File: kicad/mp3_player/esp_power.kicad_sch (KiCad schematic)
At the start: 12 parts, among them J1 Conn_USB_C_Socket, U5 AMS1117-3.3

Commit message: [ADD] an initial set of libraries to depressed to do their own job
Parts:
- renumbered C3 to C4, C4 to C5, C5 to C6, C6 to C7, C7 to C8, J1 to J2, R6 to R11, R7 to R12, R8 to R13, R9 to R14, R10 to R15
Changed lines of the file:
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@@
 		(dnp no)
 		(fields_autoplaced yes)
-		(property "Reference" "#PWR016"
+		(property "Reference" "#PWR019"
 			(at 43.18 78.74 0)
 			(hide yes)
@@
 			(project "mp3_player"
 				(path "/0f0043d3-9467-400d-886a-57a73f910f34/68afa0b0-fbce-4e06-b0d1-6752d3bde468"
-					(reference "#PWR016")
+					(reference "#PWR019")
 					(unit 1)
 				)
@@
 		(in_pos_files yes)
 		(dnp no)
-		(property "Reference" "R8"
+		(property "Reference" "R13"
 			(at 61.976 48.514 0)
 			(show_name no)
@@
 			(project "mp3_player"
 				(path "/0f0043d3-9467-400d-886a-57a73f910f34/68afa0b0-fbce-4e06-b0d1-6752d3bde468"
-					(reference "R8")
+					(reference "R13")
 					(unit 1)
 				)
@@
 		(dnp no)
 		(fields_autoplaced yes)
-		(property "Reference" "#PWR017"
+		(property "Reference" "#PWR020"
 			(at 73.66 40.64 0)
 			(hide yes)
@@
 			(project "mp3_player"
 				(path "/0f0043d3-9467-400d-886a-57a73f910f34/68afa0b0-fbce-4e06-b0d1-6752d3bde468"
-					(reference "#PWR017")
+					(reference "#PWR020")
 					(unit 1)
 				)
@@
 		(dnp no)
 		(fields_autoplaced yes)
-		(property "Reference" "R6"
+		(property "Reference" "R11"
 			(at 54.61 63.5 0)
 			(show_name no)
@@
 			(project "mp3_player"
 				(path "/0f0043d3-9467-400d-886a-57a73f910f34/68afa0b0-fbce-4e06-b0d1-6752d3bde468"
-					(reference "R6")
+					(reference "R11")
 					(unit 1)
 				)
@@
 		(dnp no)
 		(fields_autoplaced yes)
-		(property "Reference" "#PWR019"
+		(property "Reference" "#PWR022"
 			(at 74.93 31.75 0)
 			(hide yes)
@@
 			(project "mp3_player"
 				(path "/0f0043d3-9467-400d-886a-57a73f910f34/68afa0b0-fbce-4e06-b0d1-6752d3bde468"
-					(reference "#PWR019")
+					(reference "#PWR022")
 					(unit 1)
 				)
@@
 		(in_pos_files yes)
 		(dnp no)
-		(property "Reference" "C3"
+		(property "Reference" "C4"
 			(at 54.61 77.47 0)
 			(show_name no)
@@
 			(project "mp3_player"
 				(path "/0f0043d3-9467-400d-886a-57a73f910f34/68afa0b0-fbce-4e06-b0d1-6752d3bde468"
-					(reference "C3")
+					(reference "C4")
 					(unit 1)
 				)
@@
 		(dnp no)
 		(fields_autoplaced yes)
-		(property "Reference" "J1"
+		(property "Reference" "J2"
 			(at 25.4 49.5299 0)
 			(show_name no)
@@
 			(project "mp3_player"
 				(path "/0f0043d3-9467-400d-886a-57a73f910f34/68afa0b0-fbce-4e06-b0d1-6752d3bde468"
-					(reference "J1")
+					(reference "J2")
 					(unit 1)
 				)
@@
 		(dnp no)
 		(fields_autoplaced yes)
-		(property "Reference" "#PWR020"
+		(property "Reference" "#PWR023"
 			(at 74.93 59.69 0)
 			(hide yes)
@@
 			(project "mp3_player"
 				(path "/0f0043d3-9467-400d-886a-57a73f910f34/68afa0b0-fbce-4e06-b0d1-6752d3bde468"
-					(reference "#PWR020")
+					(reference "#PWR023")
 					(unit 1)
 				)
@@
 		(dnp no)
 		(fields_autoplaced yes)
-		(property "Reference" "#PWR021"
+		(property "Reference" "#PWR024"
 			(at 85.09 76.2 0)
 			(hide yes)
@@
 			(project "mp3_player"
 				(path "/0f0043d3-9467-400d-886a-57a73f910f34/68afa0b0-fbce-4e06-b0d1-6752d3bde468"
-					(reference "#PWR021")
+					(reference "#PWR024")
 					(unit 1)
 				)
@@
 		(dnp no)
 		(fields_autoplaced yes)
-		(property "Reference" "#PWR022"
+		(property "Reference" "#PWR025"
 			(at 105.41 48.26 0)
 			(hide yes)
@@
 			(project "mp3_player"
 				(path "/0f0043d3-9467-400d-886a-57a73f910f34/68afa0b0-fbce-4e06-b0d1-6752d3bde468"
-					(reference "#PWR022")
+					(reference "#PWR025")
 					(unit 1)
 				)
@@
 		(in_pos_files yes)
 		(dnp no)
-		(property "Reference" "C4"
+		(property "Reference" "C5"
 			(at 77.47 40.64 0)
 			(show_name no)
@@
 			(project "mp3_player"
 				(path "/0f0043d3-9467-400d-886a-57a73f910f34/68afa0b0-fbce-4e06-b0d1-6752d3bde468"
-					(reference "C4")
+					(reference "C5")
 					(unit 1)
 				)
@@
 		(in_pos_files yes)
 		(dnp no)
-		(property "Reference" "C7"
+		(property "Reference" "C8"
 			(at 101.6 54.61 0)
 			(show_name no)
@@
 			(project "mp3_player"
 				(path "/0f0043d3-9467-400d-886a-57a73f910f34/68afa0b0-fbce-4e06-b0d1-6752d3bde468"
-					(reference "C7")
+					(reference "C8")
 					(unit 1)
 				)
@@
 		(in_pos_files yes)
 		(dnp no)
-		(property "Reference" "C6"
+		(property "Reference" "C7"
 			(at 97.79 67.31 0)
 			(show_name no)
@@
 			(project "mp3_player"
 				(path "/0f0043d3-9467-400d-886a-57a73f910f34/68afa0b0-fbce-4e06-b0d1-6752d3bde468"
-					(reference "C6")
+					(reference "C7")
 					(unit 1)
 				)
@@
 		(in_pos_files yes)
 		(dnp no)
-		(property "Reference" "C5"
+		(property "Reference" "C6"
 			(at 88.9 67.31 0)
 			(show_name no)
@@
 			(project "mp3_player"
 				(path "/0f0043d3-9467-400d-886a-57a73f910f34/68afa0b0-fbce-4e06-b0d1-6752d3bde468"
-					(reference "C5")
+					(reference "C6")
 					(unit 1)
 				)
@@
 		(in_pos_files yes)
 		(dnp no)
-		(property "Reference" "R10"
+		(property "Reference" "R15"
 			(at 111.78 52.07 0)
 			(show_name no)
@@
 			(project "mp3_player"
 				(path "/0f0043d3-9467-400d-886a-57a73f910f34/68afa0b0-fbce-4e06-b0d1-6752d3bde468"
-					(reference "R10")
+					(reference "R15")
 					(unit 1)
 				)
@@
 		(in_pos_files yes)
 		(dnp no)
-		(property "Reference" "R9"
+		(property "Reference" "R14"
 			(at 111.76 46.99 0)
 			(show_name no)
@@
 			(project "mp3_player"
 				(path "/0f0043d3-9467-400d-886a-57a73f910f34/68afa0b0-fbce-4e06-b0d1-6752d3bde468"
-					(reference "R9")
+					(reference "R14")
 					(unit 1)
 				)
@@
 		(in_pos_files yes)
 		(dnp no)
-		(property "Reference" "R7"
+		(property "Reference" "R12"
 			(at 62.23 39.116 0)
 			(show_name no)
@@
 			(project "mp3_player"
 				(path "/0f0043d3-9467-400d-886a-57a73f910f34/68afa0b0-fbce-4e06-b0d1-6752d3bde468"
-					(reference "R7")
+					(reference "R12")
 					(unit 1)
 				)
@@
 		(dnp no)
 		(fields_autoplaced yes)
-		(property "Reference" "#PWR018"
+		(property "Reference" "#PWR021"
 			(at 73.66 43.18 0)
 			(hide yes)
@@
 			(project "mp3_player"
 				(path "/0f0043d3-9467-400d-886a-57a73f910f34/68afa0b0-fbce-4e06-b0d1-6752d3bde468"
-					(reference "#PWR018")
-					(unit 1)
-				)
+					(reference "#PWR021")
+					(unit 1)
+				)

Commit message: [UPDATE] the desing of the schematic to use the current audio module
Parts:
- renumbered C4 to C2, C5 to C3, C6 to C4, C7 to C5, C8 to C6
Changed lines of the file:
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@@
 		(dnp no)
 		(fields_autoplaced yes)
-		(property "Reference" "#PWR019"
+		(property "Reference" "#PWR017"
 			(at 43.18 78.74 0)
 			(hide yes)
@@
 			(project "mp3_player"
 				(path "/0f0043d3-9467-400d-886a-57a73f910f34/68afa0b0-fbce-4e06-b0d1-6752d3bde468"
-					(reference "#PWR019")
+					(reference "#PWR017")
 					(unit 1)
 				)
@@
 		(dnp no)
 		(fields_autoplaced yes)
-		(property "Reference" "#PWR020"
+		(property "Reference" "#PWR018"
 			(at 73.66 40.64 0)
 			(hide yes)
@@
 			(project "mp3_player"
 				(path "/0f0043d3-9467-400d-886a-57a73f910f34/68afa0b0-fbce-4e06-b0d1-6752d3bde468"
-					(reference "#PWR020")
+					(reference "#PWR018")
 					(unit 1)
 				)
@@
 		(dnp no)
 		(fields_autoplaced yes)
-		(property "Reference" "#PWR022"
+		(property "Reference" "#PWR020"
 			(at 74.93 31.75 0)
 			(hide yes)
@@
 			(project "mp3_player"
 				(path "/0f0043d3-9467-400d-886a-57a73f910f34/68afa0b0-fbce-4e06-b0d1-6752d3bde468"
-					(reference "#PWR022")
+					(reference "#PWR020")
 					(unit 1)
 				)
@@
 		(in_pos_files yes)
 		(dnp no)
-		(property "Reference" "C4"
+		(property "Reference" "C2"
 			(at 54.61 77.47 0)
 			(show_name no)
@@
 			(project "mp3_player"
 				(path "/0f0043d3-9467-400d-886a-57a73f910f34/68afa0b0-fbce-4e06-b0d1-6752d3bde468"
-					(reference "C4")
+					(reference "C2")
 					(unit 1)
 				)
@@
 		(dnp no)
 		(fields_autoplaced yes)
-		(property "Reference" "#PWR023"
+		(property "Reference" "#PWR021"
 			(at 74.93 59.69 0)
 			(hide yes)
@@
 			(project "mp3_player"
 				(path "/0f0043d3-9467-400d-886a-57a73f910f34/68afa0b0-fbce-4e06-b0d1-6752d3bde468"
-					(reference "#PWR023")
+					(reference "#PWR021")
 					(unit 1)
 				)
@@
 		(dnp no)
 		(fields_autoplaced yes)
-		(property "Reference" "#PWR024"
+		(property "Reference" "#PWR022"
 			(at 85.09 76.2 0)
 			(hide yes)
@@
 			(project "mp3_player"
 				(path "/0f0043d3-9467-400d-886a-57a73f910f34/68afa0b0-fbce-4e06-b0d1-6752d3bde468"
-					(reference "#PWR024")
+					(reference "#PWR022")
 					(unit 1)
 				)
@@
 		(dnp no)
 		(fields_autoplaced yes)
-		(property "Reference" "#PWR025"
+		(property "Reference" "#PWR023"
 			(at 105.41 48.26 0)
 			(hide yes)
@@
 			(project "mp3_player"
 				(path "/0f0043d3-9467-400d-886a-57a73f910f34/68afa0b0-fbce-4e06-b0d1-6752d3bde468"
-					(reference "#PWR025")
+					(reference "#PWR023")
 					(unit 1)
 				)
@@
 		(in_pos_files yes)
 		(dnp no)
-		(property "Reference" "C5"
+		(property "Reference" "C3"
 			(at 77.47 40.64 0)
 			(show_name no)
@@
 			(project "mp3_player"
 				(path "/0f0043d3-9467-400d-886a-57a73f910f34/68afa0b0-fbce-4e06-b0d1-6752d3bde468"
-					(reference "C5")
+					(reference "C3")
 					(unit 1)
 				)
@@
 		(in_pos_files yes)
 		(dnp no)
-		(property "Reference" "C8"
+		(property "Reference" "C6"
 			(at 101.6 54.61 0)
 			(show_name no)
@@
 			(project "mp3_player"
 				(path "/0f0043d3-9467-400d-886a-57a73f910f34/68afa0b0-fbce-4e06-b0d1-6752d3bde468"
-					(reference "C8")
+					(reference "C6")
 					(unit 1)
 				)
@@
 		(in_pos_files yes)
 		(dnp no)
-		(property "Reference" "C7"
+		(property "Reference" "C5"
 			(at 97.79 67.31 0)
 			(show_name no)
@@
 			(project "mp3_player"
 				(path "/0f0043d3-9467-400d-886a-57a73f910f34/68afa0b0-fbce-4e06-b0d1-6752d3bde468"
-					(reference "C7")
+					(reference "C5")
 					(unit 1)
 				)
@@
 		(in_pos_files yes)
 		(dnp no)
-		(property "Reference" "C6"
+		(property "Reference" "C4"
 			(at 88.9 67.31 0)
 			(show_name no)
@@
 			(project "mp3_player"
 				(path "/0f0043d3-9467-400d-886a-57a73f910f34/68afa0b0-fbce-4e06-b0d1-6752d3bde468"
-					(reference "C6")
+					(reference "C4")
 					(unit 1)
 				)
@@
 		(dnp no)
 		(fields_autoplaced yes)
-		(property "Reference" "#PWR021"
+		(property "Reference" "#PWR019"
 			(at 73.66 43.18 0)
 			(hide yes)
@@
 			(project "mp3_player"
 				(path "/0f0043d3-9467-400d-886a-57a73f910f34/68afa0b0-fbce-4e06-b0d1-6752d3bde468"
-					(reference "#PWR021")
-					(unit 1)
-				)
+					(reference "#PWR019")
+					(unit 1)
+				)

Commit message: [ADD] lcd segment displays to the project
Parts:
- renumbered J2 to J4
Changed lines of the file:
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@@
 		(dnp no)
 		(fields_autoplaced yes)
-		(property "Reference" "#PWR017"
+		(property "Reference" "#PWR020"
 			(at 43.18 78.74 0)
 			(hide yes)
@@
 			(project "mp3_player"
 				(path "/0f0043d3-9467-400d-886a-57a73f910f34/68afa0b0-fbce-4e06-b0d1-6752d3bde468"
-					(reference "#PWR017")
+					(reference "#PWR020")
 					(unit 1)
 				)
@@
 		(dnp no)
 		(fields_autoplaced yes)
-		(property "Reference" "#PWR018"
+		(property "Reference" "#PWR021"
 			(at 73.66 40.64 0)
 			(hide yes)
@@
 			(project "mp3_player"
 				(path "/0f0043d3-9467-400d-886a-57a73f910f34/68afa0b0-fbce-4e06-b0d1-6752d3bde468"
-					(reference "#PWR018")
+					(reference "#PWR021")
 					(unit 1)
 				)
@@
 		(dnp no)
 		(fields_autoplaced yes)
-		(property "Reference" "#PWR020"
+		(property "Reference" "#PWR023"
 			(at 74.93 31.75 0)
 			(hide yes)
@@
 			(project "mp3_player"
 				(path "/0f0043d3-9467-400d-886a-57a73f910f34/68afa0b0-fbce-4e06-b0d1-6752d3bde468"
-					(reference "#PWR020")
+					(reference "#PWR023")
 					(unit 1)
 				)
@@
 		(dnp no)
 		(fields_autoplaced yes)
-		(property "Reference" "J2"
+		(property "Reference" "J4"
 			(at 25.4 49.5299 0)
 			(show_name no)
@@
 			(project "mp3_player"
 				(path "/0f0043d3-9467-400d-886a-57a73f910f34/68afa0b0-fbce-4e06-b0d1-6752d3bde468"
-					(reference "J2")
+					(reference "J4")
 					(unit 1)
 				)
@@
 		(dnp no)
 		(fields_autoplaced yes)
-		(property "Reference" "#PWR021"
+		(property "Reference" "#PWR024"
 			(at 74.93 59.69 0)
 			(hide yes)
@@
 			(project "mp3_player"
 				(path "/0f0043d3-9467-400d-886a-57a73f910f34/68afa0b0-fbce-4e06-b0d1-6752d3bde468"
-					(reference "#PWR021")
+					(reference "#PWR024")
 					(unit 1)
 				)
@@
 		(dnp no)
 		(fields_autoplaced yes)
-		(property "Reference" "#PWR022"
+		(property "Reference" "#PWR025"
 			(at 85.09 76.2 0)
 			(hide yes)
@@
 			(project "mp3_player"
 				(path "/0f0043d3-9467-400d-886a-57a73f910f34/68afa0b0-fbce-4e06-b0d1-6752d3bde468"
-					(reference "#PWR022")
+					(reference "#PWR025")
 					(unit 1)
 				)
@@
 		(dnp no)
 		(fields_autoplaced yes)
-		(property "Reference" "#PWR023"
+		(property "Reference" "#PWR026"
 			(at 105.41 48.26 0)
 			(hide yes)
@@
 			(project "mp3_player"
 				(path "/0f0043d3-9467-400d-886a-57a73f910f34/68afa0b0-fbce-4e06-b0d1-6752d3bde468"
-					(reference "#PWR023")
+					(reference "#PWR026")
 					(unit 1)
 				)
@@
 		(dnp no)
 		(fields_autoplaced yes)
-		(property "Reference" "#PWR019"
+		(property "Reference" "#PWR022"
 			(at 73.66 43.18 0)
 			(hide yes)
@@
 			(project "mp3_player"
 				(path "/0f0043d3-9467-400d-886a-57a73f910f34/68afa0b0-fbce-4e06-b0d1-6752d3bde468"
-					(reference "#PWR019")
-					(unit 1)
-				)
+					(reference "#PWR022")
+					(unit 1)
+				)

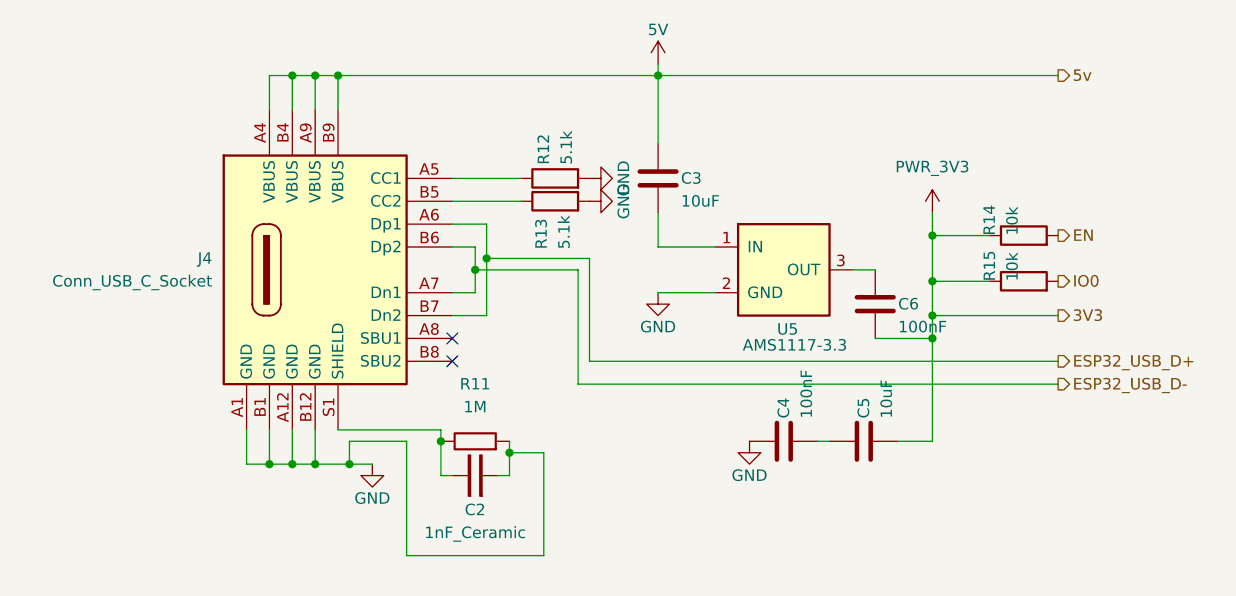
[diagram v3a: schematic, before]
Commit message: [UPDATE] the schematic to include the power help to avoid a crash or lcd corruption due to brown outs
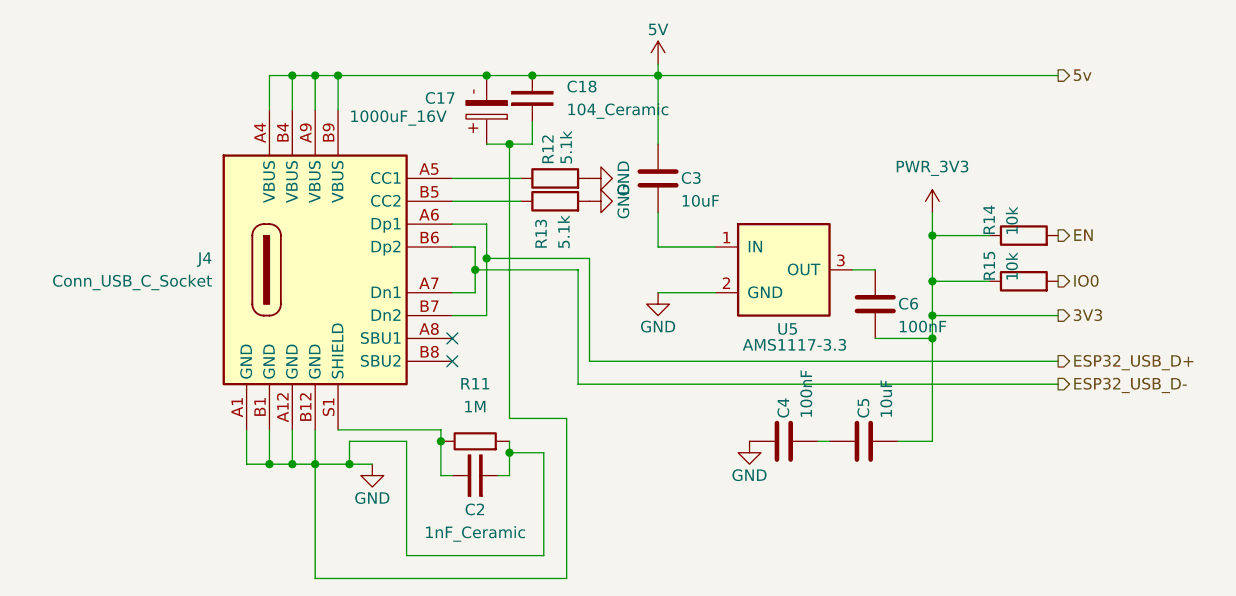
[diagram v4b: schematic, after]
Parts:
- added C17: 1000uF_16V, Capacitor_THT:CP_Radial_D10.0mm_P5.00mm, symbol PCM_SL_Capacitors:1000uF_16V
- added C18: 104_Ceramic, Capacitor_THT:C_Disc_D5.0mm_W2.5mm_P2.50mm, symbol PCM_SL_Capacitors:104_Ceramic
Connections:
- net 5V: now also C17.2, C18.2
- net GND: now also C17.1, C18.1
